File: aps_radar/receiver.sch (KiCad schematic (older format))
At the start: 2 parts

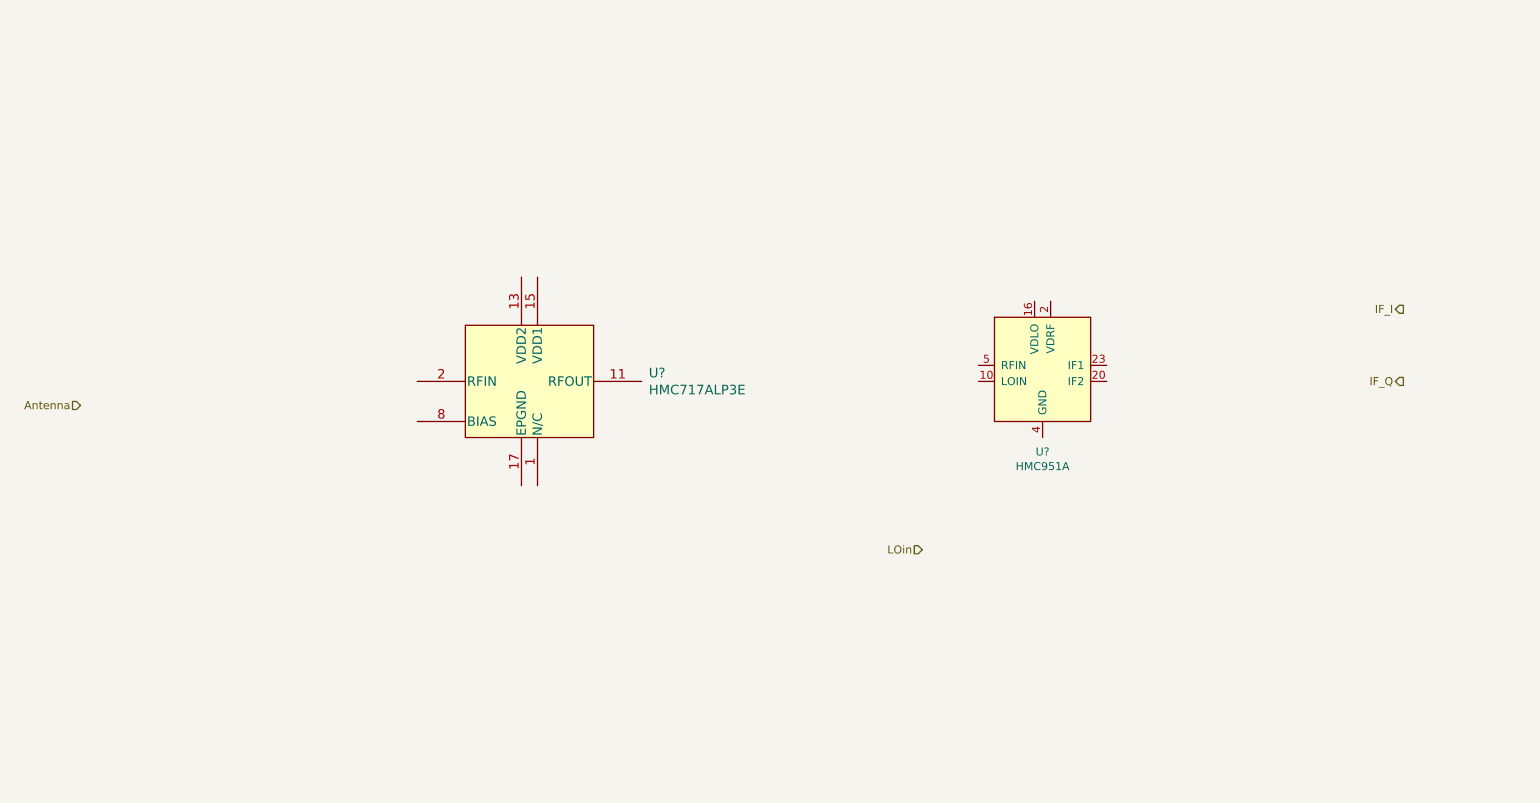
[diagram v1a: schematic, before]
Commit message: Integrated transmitter and receiver.  Need to add ferrite beads and power supply module.
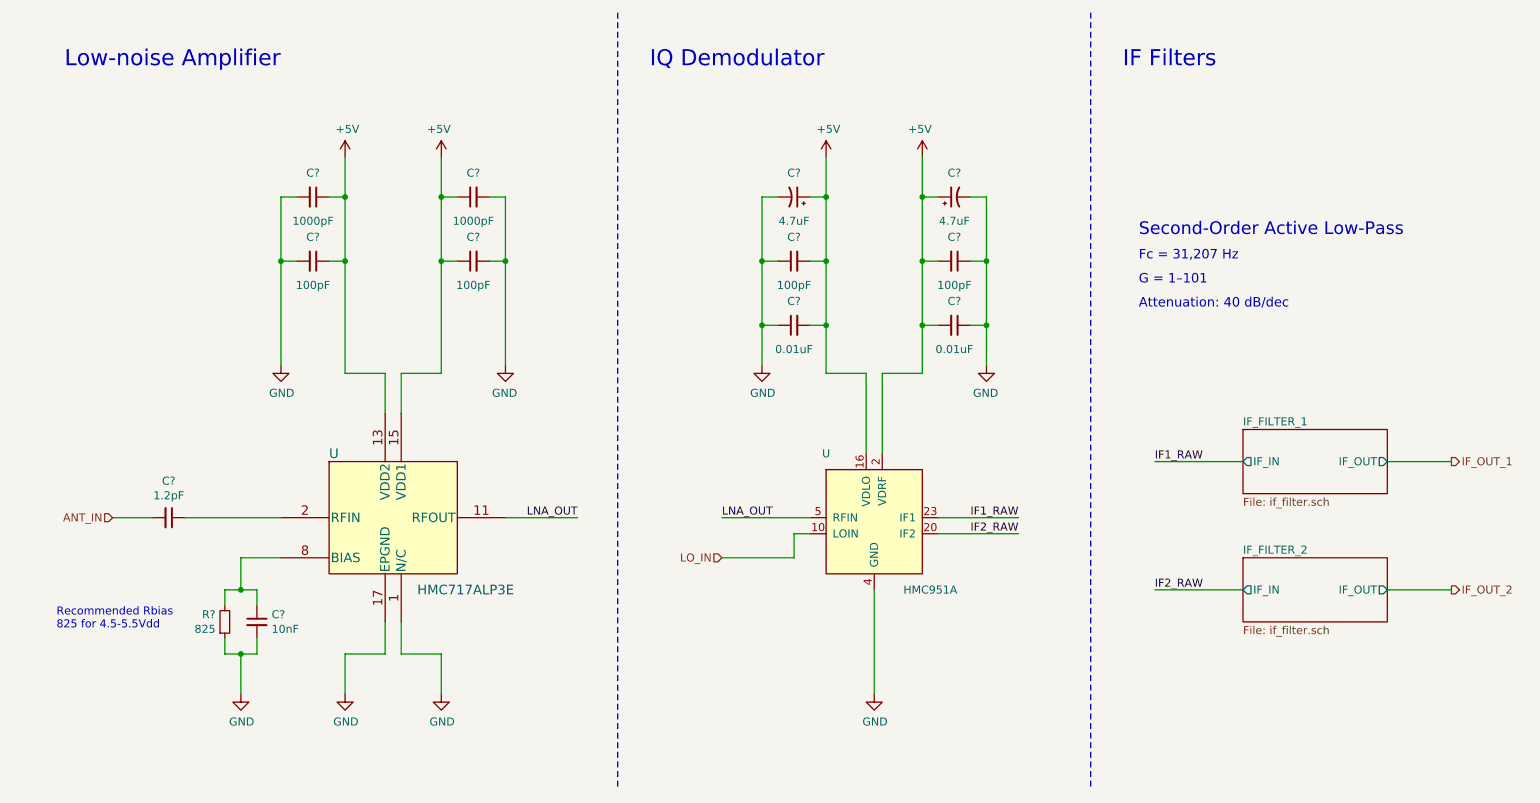
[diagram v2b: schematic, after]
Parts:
- added C?: 1.2pF, symbol Device:C_Small
- added C? (x4): 100pF, symbol Device:C_Small
- added C? (x2): 0.01uF, symbol Device:C_Small
- added C?: 10nF, symbol Device:C_Small
- added C? (x2): 1000pF, symbol Device:C_Small
- added C? (x2): 4.7uF, symbol Device:CP1_Small
- added R?: 825, symbol Device:R_Small
- gave numbers to parts that had none: 1
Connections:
- net LO_IN: now reaches U.10 (LOIN)
- net GND: now reaches U.11 (GND), U.19 (GND), U.21 (GND), U.22 (GND), U.24 (GND), U.25 (GND), U.4 (GND), U.6 (GND), U.9 (GND)
- net GND: now also U.1 (N/C), U.10 (N/C), U.12 (N/C), U.14 (N/C), U.16 (N/C), U.17 (EPGND), U.3 (N/C), U.4 (N/C), U.5 (N/C), U.6 (N/C), U.7 (N/C), U.9 (N/C), C?.1, C?.1, C?.1, C?.1, C?.2, C?.2, C?.2, C?.2, C?.2, C?.2, C?.2, R?.1
- net +5V: now reaches U.16 (VDLO)
- net +5V: now also U.13 (VDD2), U.15 (VDD1), U.2 (VDRF), C?.1, C?.1, C?.1, C?.1, C?.1, C?.1, C?.2, C?.2, C?.2, C?.2
- net IF2_RAW: now reaches U.20 (IF2)
- net IF1_RAW: now reaches U.23 (IF1)
- net LNA_OUT: now reaches U.5 (RFIN)
- net LNA_OUT: now also U.11 (RFOUT)
- net at U.2 (RFIN): now also C?.1
- net at U.8 (BIAS): now also C?.1, R?.2
- new net ANT_IN: C?.2
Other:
- note added: "Attenuation: 40 dB/dec"
- note added: "Fc = 31,207 Hz"
- note added: "G = 1–101"
- note added: "IF Filters"
- note added: "IQ Demodulator"
- note added: "Low-noise Amplifier"
- note added: "Recommended Rbias \n825 for 4.5-5.5Vdd"
- note added: "Second-Order Active Low-Pass"
- moved on the sheet: U
